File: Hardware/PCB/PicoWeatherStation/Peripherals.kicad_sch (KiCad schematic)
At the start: 22 parts, among them U3 nRF24L01+, U4 GY-BME280, U5 ZR-3A

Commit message: Update the PCB
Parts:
- added SW2, SW3, SW4, SW5, SW6, SW7: SW_PICO_RST, Button_Switch_SMD:SW_Push_1P1T_NO_6x6mm_H9.5mm, symbol Switch:SW_Push
- added U6: 47L16, Package_SO:SOIC-8_3.9x4.9mm_P1.27mm, symbol Memory_NVRAM:47L16
- added U7: MCP7940N-xSN, Package_SO:SOIC-8_3.9x4.9mm_P1.27mm, symbol Timer_RTC:MCP7940N-xSN
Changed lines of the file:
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@@
+    (pin "2")
+  )
+  (symbol (lib_id "Switch:SW_Push") (at 231.14 55.88 0) (unit 1)
+    (in_bom yes) (on_board yes) (fields_autoplaced)
+    (property "Reference" "SW2" (id 0) (at 231.14 48.26 0))
+    (property "Value" "SW_PICO_RST" (id 1) (at 231.14 50.8 0))
+    (property "Footprint" "Button_Switch_SMD:SW_Push_1P1T_NO_6x6mm_H9.5mm" (id 2) (at 231.14 50.8 0)
+      (effects (font (size 1.27 1.27)) hide)
+    )
+    (property "Datasheet" "~" (id 3) (at 231.14 50.8 0)
+      (effects (font (size 1.27 1.27)) hide)
+    )
+    (pin "1")
     (pin "2")
   )
@@
     (pin "2")
   )
+  (symbol (lib_id "Switch:SW_Push") (at 231.14 78.74 0) (unit 1)
+    (in_bom yes) (on_board yes) (fields_autoplaced)
+    (property "Reference" "SW4" (id 0) (at 231.14 71.12 0))
+    (property "Value" "SW_PICO_RST" (id 1) (at 231.14 73.66 0))
+    (property "Footprint" "Button_Switch_SMD:SW_Push_1P1T_NO_6x6mm_H9.5mm" (id 2) (at 231.14 73.66 0)
+      (effects (font (size 1.27 1.27)) hide)
+    )
+    (property "Datasheet" "~" (id 3) (at 231.14 73.66 0)
+      (effects (font (size 1.27 1.27)) hide)
+    )
+    (pin "1")
+    (pin "2")
+  )
   (symbol (lib_id "Device:C") (at 54.61 36.83 0) (unit 1)
     (in_bom yes) (on_board yes) (fields_autoplaced)
@@
     )
     (pin "1")
+  )
+  (symbol (lib_id "Switch:SW_Push") (at 231.14 113.03 0) (unit 1)
+    (in_bom yes) (on_board yes) (fields_autoplaced)
+    (property "Reference" "SW7" (id 0) (at 231.14 105.41 0))
+    (property "Value" "SW_PICO_RST" (id 1) (at 231.14 107.95 0))
+    (property "Footprint" "Button_Switch_SMD:SW_Push_1P1T_NO_6x6mm_H9.5mm" (id 2) (at 231.14 107.95 0)
+      (effects (font (size 1.27 1.27)) hide)
+    )
+    (property "Datasheet" "~" (id 3) (at 231.14 107.95 0)
+      (effects (font (size 1.27 1.27)) hide)
+    )
+    (pin "1")
+    (pin "2")
   )
   (symbol (lib_id "Device:R") (at 83.82 49.53 90) (unit 1)
@@
     (pin "8")
   )
+  (symbol (lib_id "Timer_RTC:MCP7940N-xSN") (at 163.83 102.87 0) (unit 1)
+    (in_bom yes) (on_board yes) (fields_autoplaced)
+    (property "Reference" "U7" (id 0) (at 165.8494 113.03 0)
+      (effects (font (size 1.27 1.27)) (justify left))
+    )
+    (property "Value" "MCP7940N-xSN" (id 1) (at 165.8494 115.57 0)
+      (effects (font (size 1.27 1.27)) (justify left))
+    )
+    (property "Footprint" "Package_SO:SOIC-8_3.9x4.9mm_P1.27mm" (id 2) (at 163.83 102.87 0)
+      (effects (font (size 1.27 1.27)) hide)
+    )
+    (property "Datasheet" "http://ww1.microchip.com/downloads/en/DeviceDoc/20005010F.pdf" (id 3) (at 163.83 102.87 0)
+      (effects (font (size 1.27 1.27)) hide)
+    )
+    (pin "1")
+    (pin "2")
+    (pin "3")
+    (pin "4")
+    (pin "5")
+    (pin "6")
+    (pin "7")
+    (pin "8")
+  )
   (symbol (lib_id "Device:R") (at 83.82 46.99 90) (unit 1)
     (in_bom yes) (on_board yes)
@@
     (pin "2")
   )
+  (symbol (lib_id "Switch:SW_Push") (at 231.14 101.6 0) (unit 1)
+    (in_bom yes) (on_board yes) (fields_autoplaced)
+    (property "Reference" "SW6" (id 0) (at 231.14 93.98 0))
+    (property "Value" "SW_PICO_RST" (id 1) (at 231.14 96.52 0))
+    (property "Footprint" "Button_Switch_SMD:SW_Push_1P1T_NO_6x6mm_H9.5mm" (id 2) (at 231.14 96.52 0)
+      (effects (font (size 1.27 1.27)) hide)
+    )
+    (property "Datasheet" "~" (id 3) (at 231.14 96.52 0)
+      (effects (font (size 1.27 1.27)) hide)
+    )
+    (pin "1")
+    (pin "2")
+  )
   (symbol (lib_id "Device:C") (at 54.61 91.44 0) (unit 1)
     (in_bom yes) (on_board yes) (fields_autoplaced)
@@
     (pin "2")
   )
+  (symbol (lib_id "Switch:SW_Push") (at 231.14 90.17 0) (unit 1)
+    (in_bom yes) (on_board yes) (fields_autoplaced)
+    (property "Reference" "SW5" (id 0) (at 231.14 82.55 0))
+    (property "Value" "SW_PICO_RST" (id 1) (at 231.14 85.09 0))
+    (property "Footprint" "Button_Switch_SMD:SW_Push_1P1T_NO_6x6mm_H9.5mm" (id 2) (at 231.14 85.09 0)
+      (effects (font (size 1.27 1.27)) hide)
+    )
+    (property "Datasheet" "~" (id 3) (at 231.14 85.09 0)
+      (effects (font (size 1.27 1.27)) hide)
+    )
+    (pin "1")
+    (pin "2")
+  )
+  (symbol (lib_id "Switch:SW_Push") (at 231.14 67.31 0) (unit 1)
+    (in_bom yes) (on_board yes) (fields_autoplaced)
+    (property "Reference" "SW3" (id 0) (at 231.14 59.69 0))
+    (property "Value" "SW_PICO_RST" (id 1) (at 231.14 62.23 0))
+    (property "Footprint" "Button_Switch_SMD:SW_Push_1P1T_NO_6x6mm_H9.5mm" (id 2) (at 231.14 62.23 0)
+      (effects (font (size 1.27 1.27)) hide)
+    )
+    (property "Datasheet" "~" (id 3) (at 231.14 62.23 0)
+      (effects (font (size 1.27 1.27)) hide)
+    )
+    (pin "1")
+    (pin "2")
+  )
+  (symbol (lib_id "Memory_NVRAM:47L16") (at 163.83 44.45 0) (unit 1)
+    (in_bom yes) (on_board yes) (fields_autoplaced)
+    (property "Reference" "U6" (id 0) (at 165.8494 54.61 0)
+      (effects (font (size 1.27 1.27)) (justify left))
+    )
+    (property "Value" "47L16" (id 1) (at 165.8494 57.15 0)
+      (effects (font (size 1.27 1.27)) (justify left))
+    )
+    (property "Footprint" "Package_SO:SOIC-8_3.9x4.9mm_P1.27mm" (id 2) (at 163.83 55.88 0)
+      (effects (font (size 1.27 1.27)) hide)
+    )
+    (property "Datasheet" "http://ww1.microchip.com/downloads/en/DeviceDoc/20005371C.pdf" (id 3) (at 170.18 35.56 0)
+      (effects (font (size 1.27 1.27)) hide)
+    )
+    (pin "1")
+    (pin "2")
+    (pin "3")
+    (pin "4")
+    (pin "5")
+    (pin "6")
+    (pin "7")
+    (pin "8")
+  )
   (symbol (lib_id "Device:C") (at 54.61 146.05 0) (unit 1)

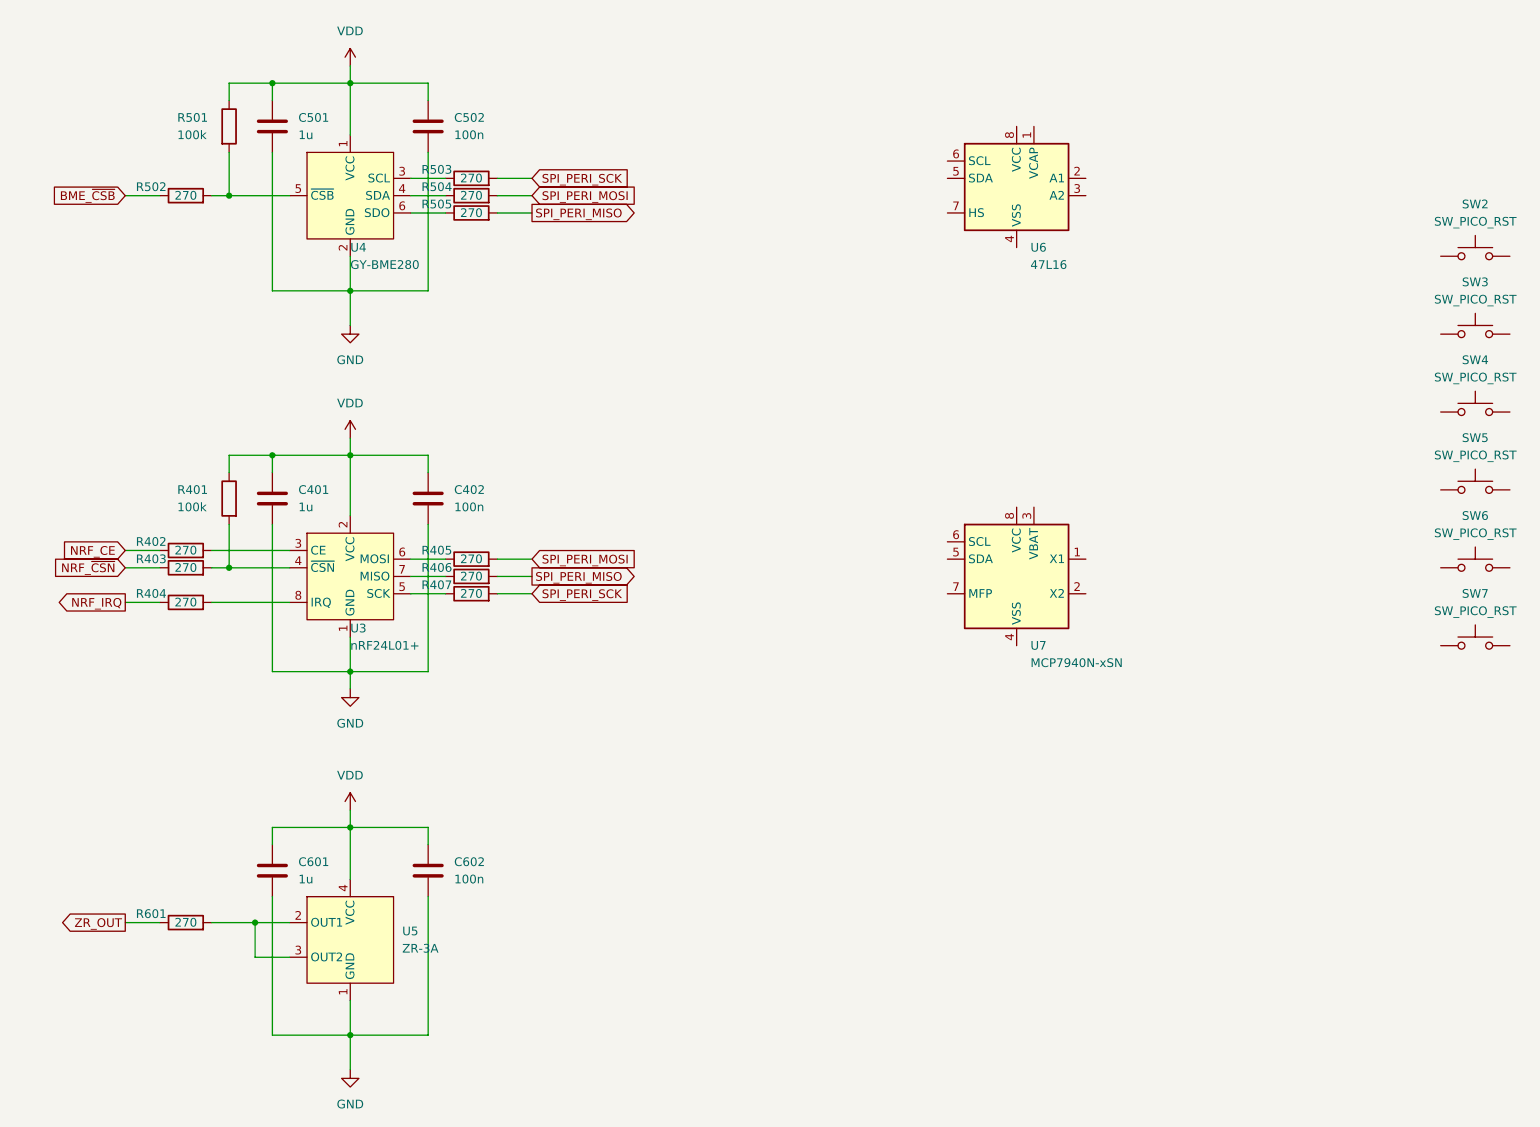
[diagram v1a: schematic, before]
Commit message: PCB: add RTC and EERAM
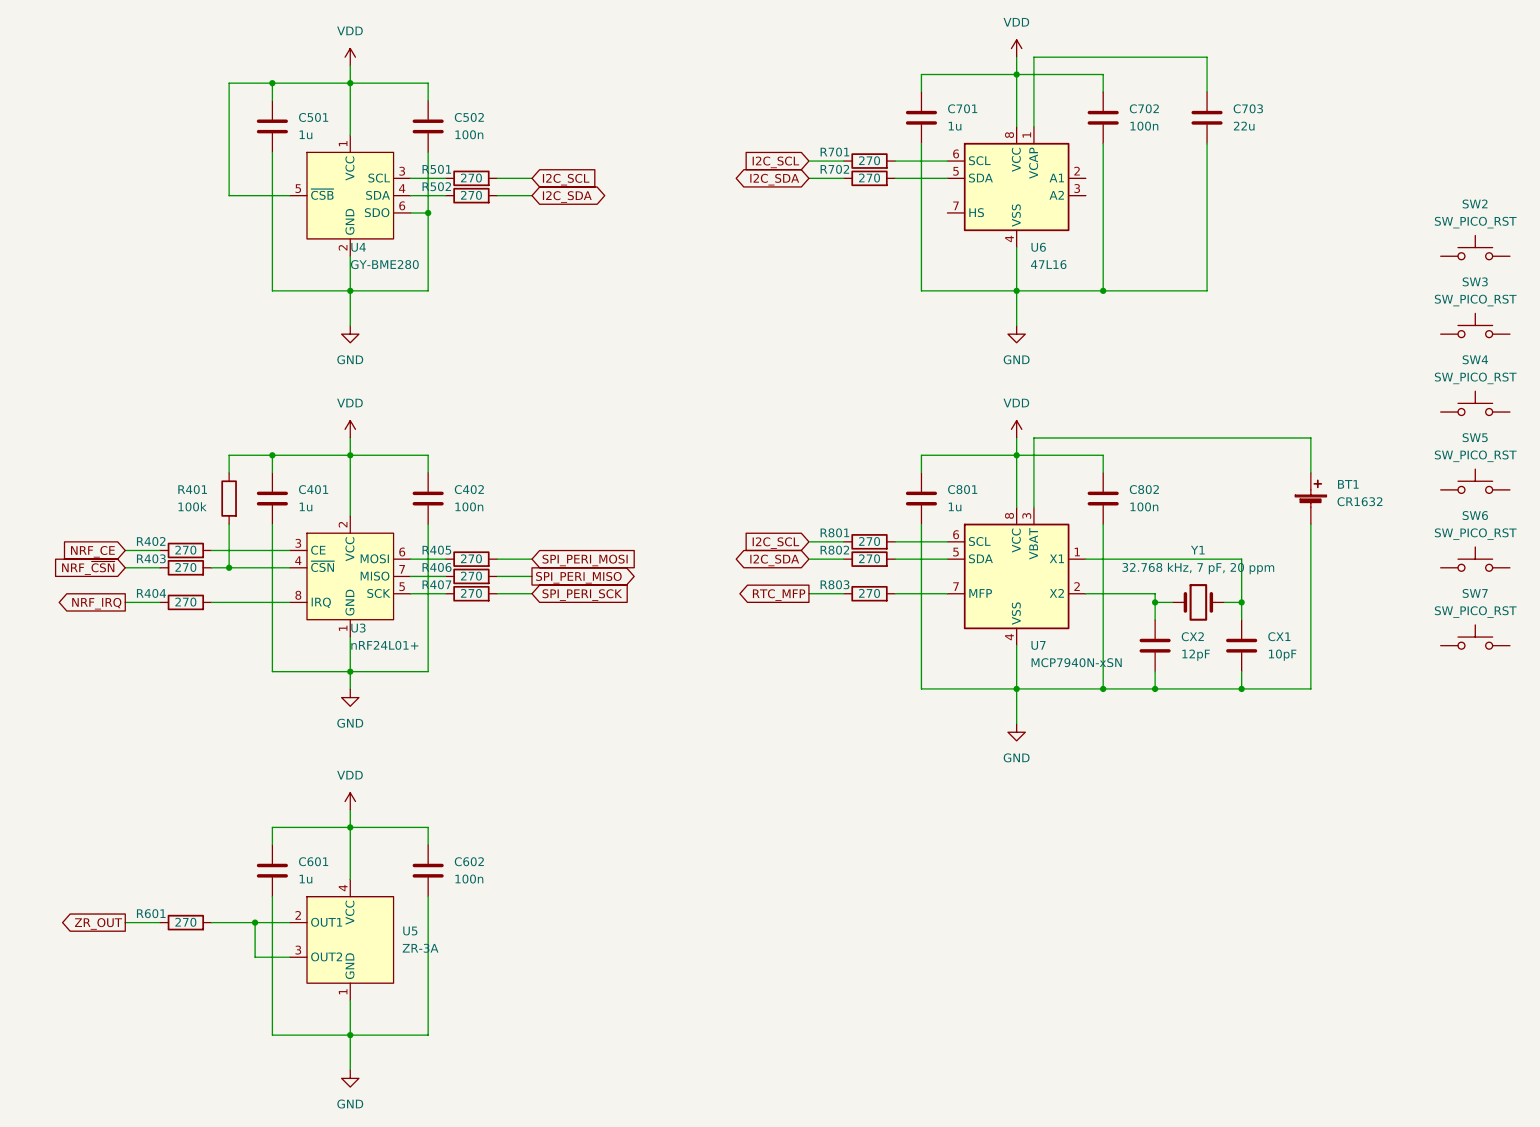
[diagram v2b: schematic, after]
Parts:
- removed R501: 100k, Resistor_SMD:R_0805_2012Metric_Pad1.20x1.40mm_HandSolder, symbol Device:R
- removed R502, R505: 270, Resistor_SMD:R_0805_2012Metric_Pad1.20x1.40mm_HandSolder, symbol Device:R
- added BT1: CR1632, PicoWeatherStation:Battery_Holder_CR1632, symbol Device:Battery_Cell
- added C701, C801: 1u, Capacitor_SMD:C_0805_2012Metric_Pad1.18x1.45mm_HandSolder, symbol Device:C
- added C702, C802: 100n, Capacitor_SMD:C_0805_2012Metric_Pad1.18x1.45mm_HandSolder, symbol Device:C
- added C703: 22u, Capacitor_SMD:C_0805_2012Metric_Pad1.18x1.45mm_HandSolder, symbol Device:C
- added CX1: 10pF, Capacitor_SMD:C_0805_2012Metric_Pad1.18x1.45mm_HandSolder, symbol Device:C
- added CX2: 12pF, Capacitor_SMD:C_0805_2012Metric_Pad1.18x1.45mm_HandSolder, symbol Device:C
- added R701, R702, R801, R802, R803: 270, Resistor_SMD:R_0805_2012Metric_Pad1.20x1.40mm_HandSolder, symbol Device:R
- added Y1: 32.768 kHz, 7 pF, 20 ppm, Crystal:Crystal_SMD_3215-2Pin_3.2x1.5mm, symbol Device:Crystal
- renumbered R503 to R501, R504 to R502
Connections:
- net GND: now also U4.6 (SDO), U6.4 (VSS), U7.4 (VSS), BT1.2 (-), C701.2, C702.2, C703.2, C801.2, C802.2, CX1.2, CX2.2
- net SPI_PERI_MOSI: no longer R502.2
- net SPI_PERI_SCK: no longer R501.2
- net VDD: now also U4.5 (~{CSB}), U6.8 (VCC), U7.8 (VCC), C701.1, C702.1, C801.1, C802.1
- net at U7.1 (X1): now also CX1.1, Y1.2
- net at U7.2 (X2): now also CX2.1, Y1.1
- net at U7.3 (VBAT): now also BT1.1 (+)
- net at U7.5 (SDA): now also R802.2
- net at U7.6 (SCL): now also R801.2
- net at U7.7 (MFP): now also R803.2
- net at U6.1 (VCAP): now also C703.1
- net at U6.5 (SDA): now also R702.2
- net at U6.6 (SCL): now also R701.2
- new net I2C_SCL: R501.2, R701.1, R801.1
- new net I2C_SDA: R502.2, R702.1, R802.1
- new net RTC_MFP: R803.1

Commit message: PCB: wire-up the keyboard
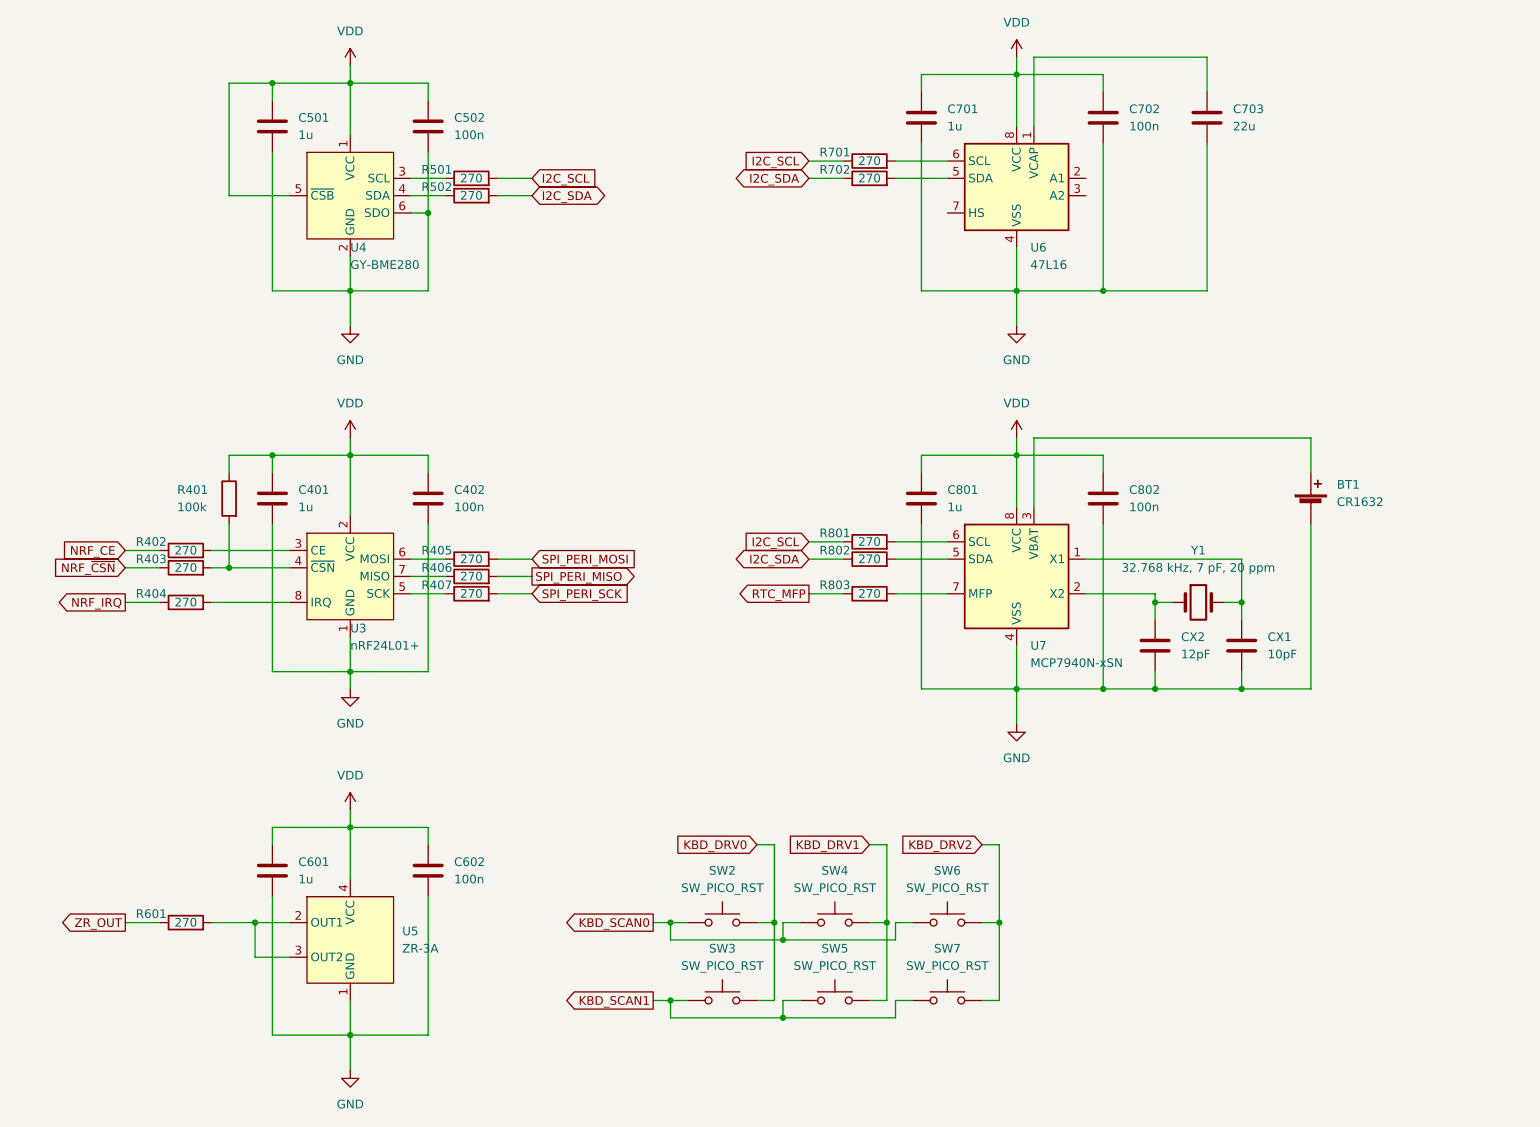
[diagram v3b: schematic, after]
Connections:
- net KBD_SCAN0: now reaches SW2.1
- net KBD_SCAN0: now also SW4.1, SW6.1
- net KBD_DRV0: now reaches SW2.2
- net KBD_DRV0: now also SW3.2
- net KBD_DRV1: now reaches SW4.2
- net KBD_DRV1: now also SW5.2
- net KBD_SCAN1: now reaches SW7.1
- net KBD_SCAN1: now also SW3.1, SW5.1
- net KBD_DRV2: now reaches SW7.2
- net KBD_DRV2: now also SW6.2
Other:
- moved on the sheet: SW2, SW3, SW4, SW5, SW6, SW7

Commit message: PCB: bigger footprint for the clock crystal
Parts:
- Y1: footprint Crystal:Crystal_SMD_3215-2Pin_3.2x1.5mm -> Crystal:Crystal_SMD_5032-2Pin_5.0x3.2mm
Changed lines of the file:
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@@
     (property "Reference" "Y1" (id 0) (at 190.5 99.06 0))
     (property "Value" "32.768 kHz, 7 pF, 20 ppm" (id 1) (at 190.5 101.6 0))
-    (property "Footprint" "Crystal:Crystal_SMD_3215-2Pin_3.2x1.5mm" (id 2) (at 190.5 106.68 0)
+    (property "Footprint" "Crystal:Crystal_SMD_5032-2Pin_5.0x3.2mm" (id 2) (at 190.5 106.68 0)
       (effects (font (size 1.27 1.27)) hide)
     )
